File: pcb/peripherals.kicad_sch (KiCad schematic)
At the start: 30 parts, among them U2 PCA9545APW, U3 HDC1080, U4 LTR-303ALS-01, U5 SGP40-D-R4

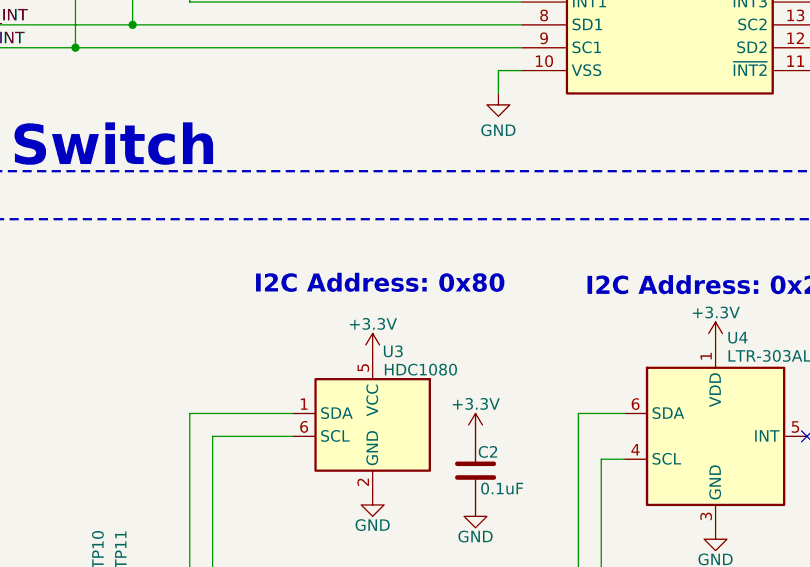
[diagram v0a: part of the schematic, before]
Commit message: Fixed LTR address from 0x80 to 0x40
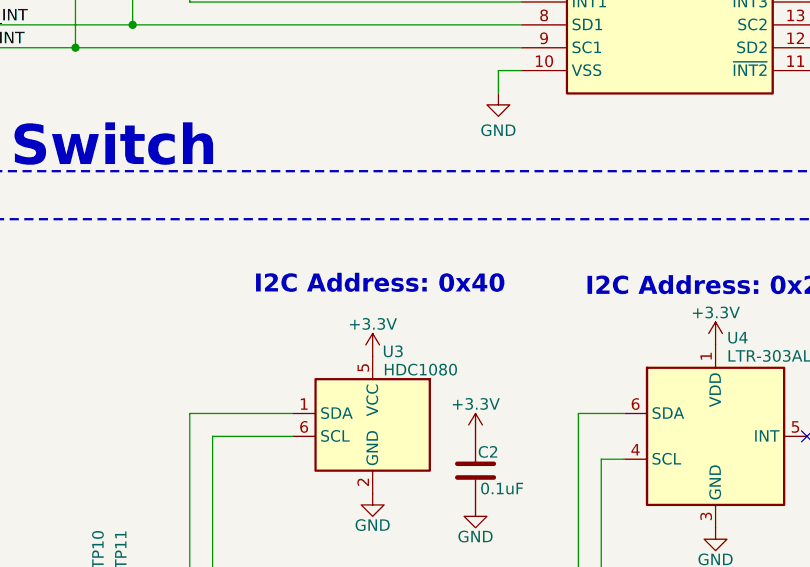
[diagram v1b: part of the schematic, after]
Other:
- note added: "I2C Address: 0x40"
- note removed: "I2C Address: 0x80"
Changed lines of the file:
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@@
 		)
 	)
-	(text "I2C Address: 0x80"
+	(text "I2C Address: 0x40"
 		(exclude_from_sim no)
 		(at 55.372 83.566 0)

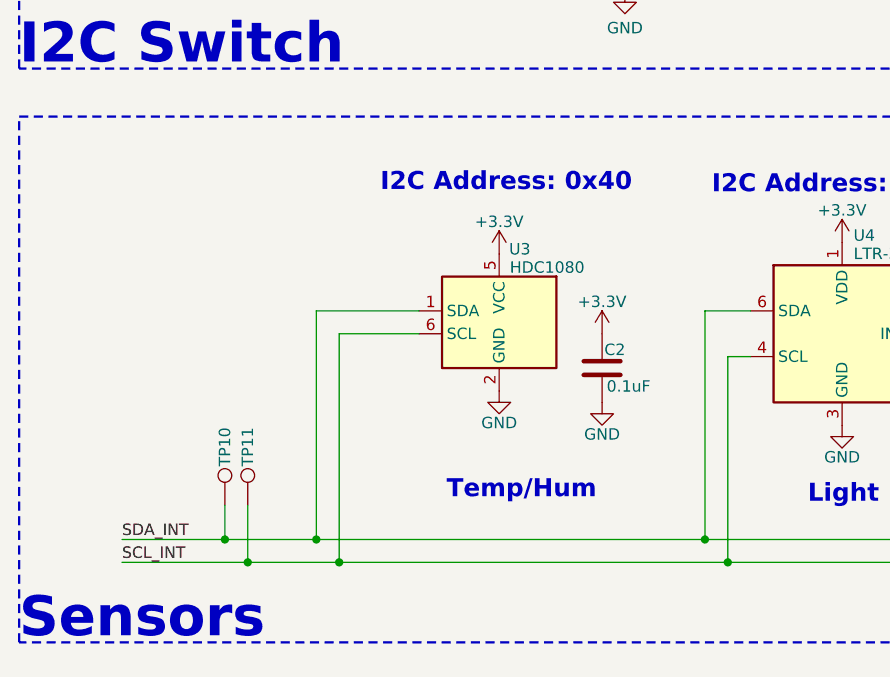
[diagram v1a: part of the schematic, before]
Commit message: Swapped temp sensor for more popular model
Changed HDC1080 for AHT20
Updated reference layer
Updated renders
Updated requirements
Fixed models
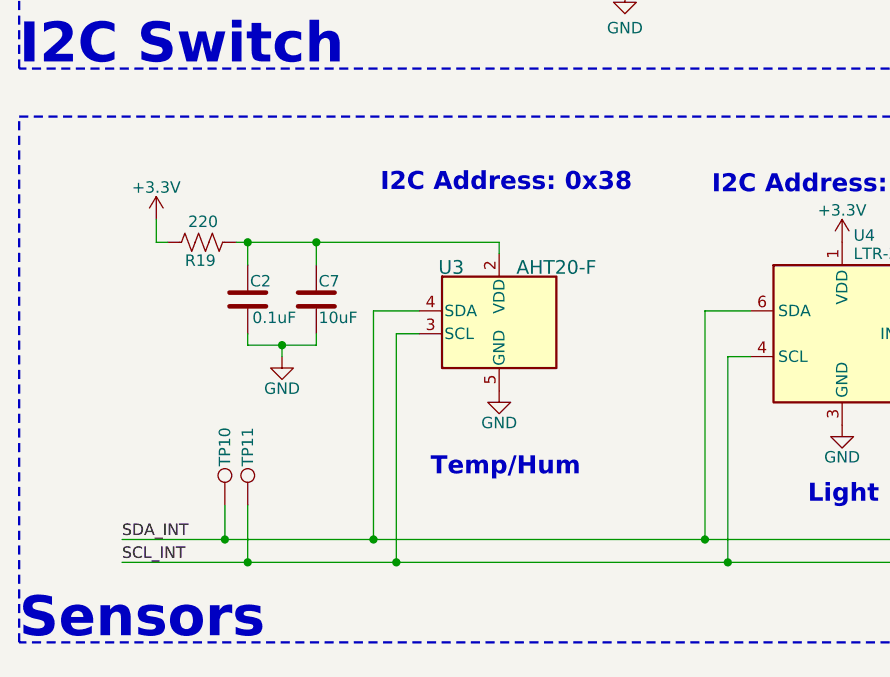
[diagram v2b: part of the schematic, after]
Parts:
- removed U3: HDC1080, CRG Makes:PWSON-N6, symbol CRG Makes:HDC1080
- added C7: 10uF, CRGM Passive:C_0603_1608Metric, symbol Device:C
- added R19: 220, CRGM Passive:R_0603_1608Metric, symbol Device:R_US
- added U3: AHT20-F, CRG Makes:AHT20, symbol CRG Makes:AHT20-F
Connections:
- net +3.3V: now also R19.1; no longer C2.1
- net GND: now also C7.2, U3.5 (GND)
- net SCL_INT: now also U3.3 (SCL)
- net SDA_INT: now also U3.4 (SDA)
- new net: C2.1, C7.1, R19.2, U3.2 (VDD)
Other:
- note added: "I2C Address: 0x38"
- note removed: "I2C Address: 0x40"
- moved on the sheet: C2

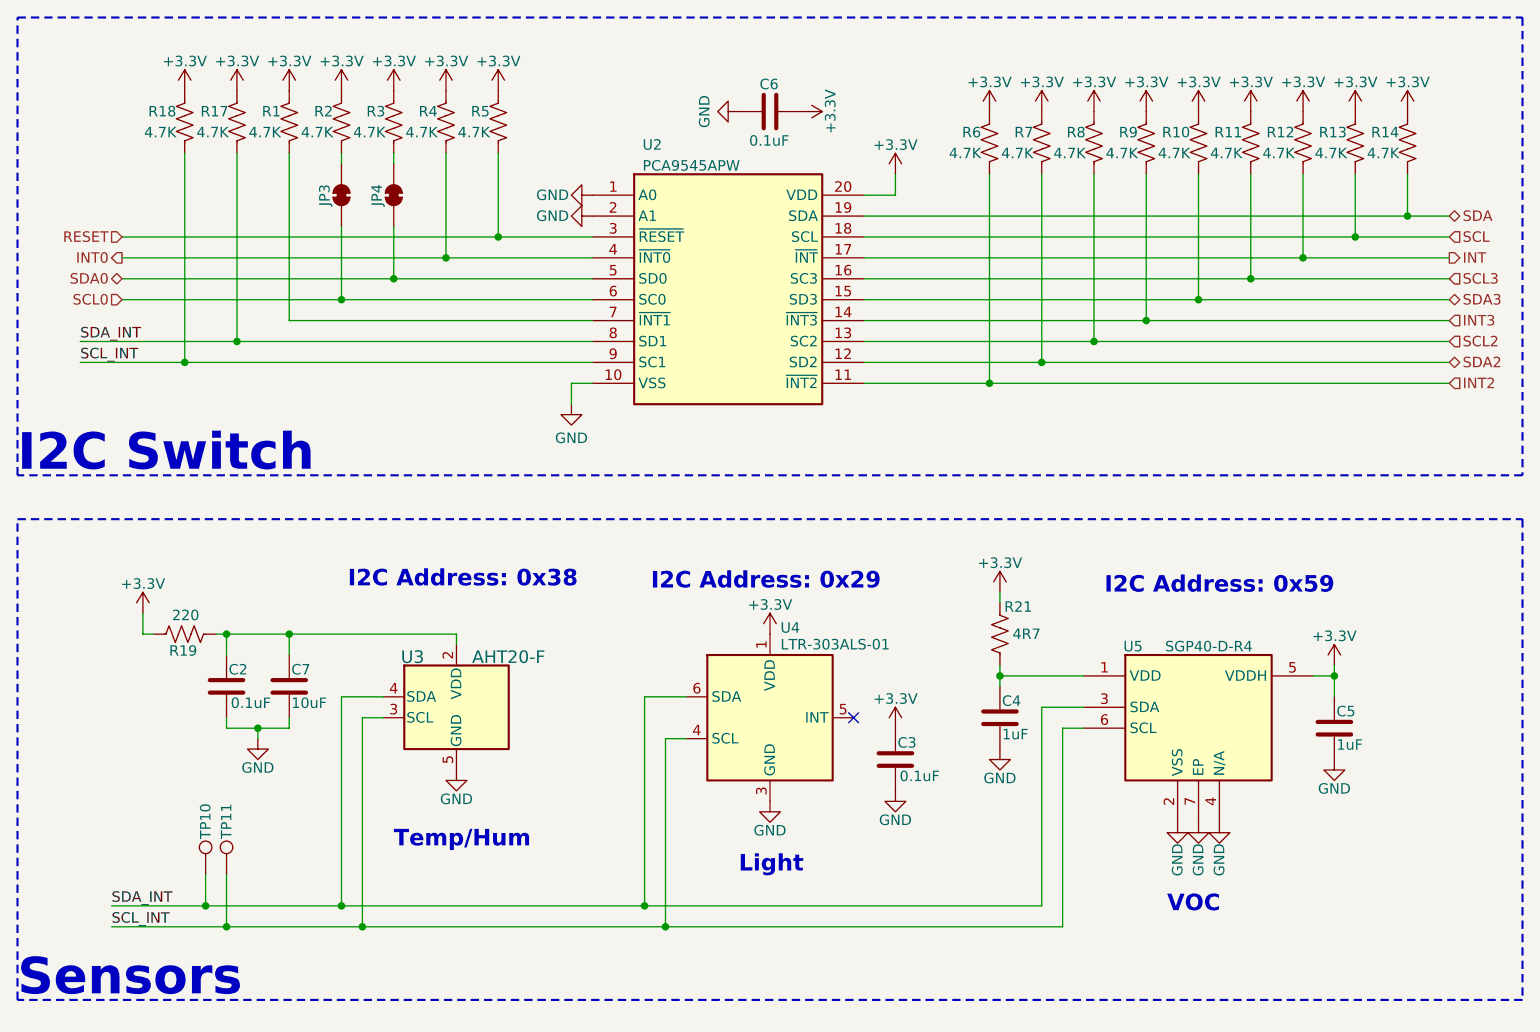
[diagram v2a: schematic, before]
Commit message: Switched back to global lables
Updated all gnd and test point symbols
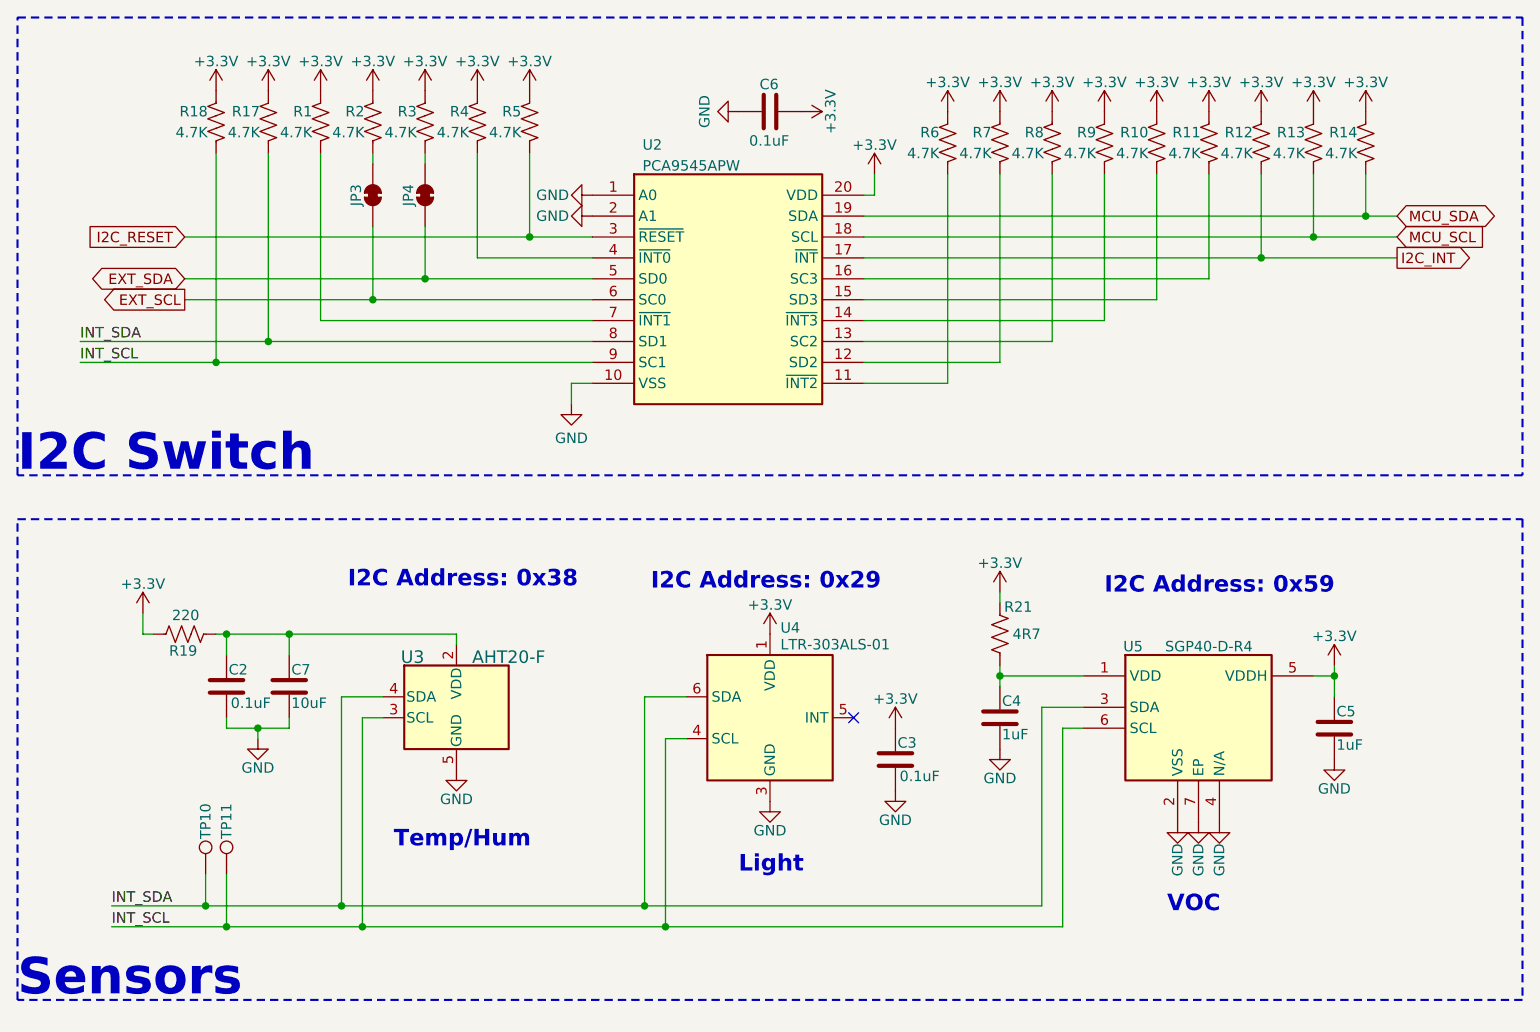
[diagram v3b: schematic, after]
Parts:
- TP10, TP11: symbol Connector:TestPoint -> CRGM Connector:TestPoint
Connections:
- net INT renamed I2C_INT
- net INT0: no longer names the net of R4.1, U2.4 (~{INT0})
- net INT2: no longer names the net of R6.1, U2.11 (~{INT2})
- net INT3: no longer names the net of R9.1, U2.14 (~{INT3})
- net RESET renamed I2C_RESET
- net SCL renamed MCU_SCL
- net SCL0 renamed EXT_SCL
- net SCL2: no longer names the net of R8.1, U2.13 (SC2)
- net SCL3: no longer names the net of R11.1, U2.16 (SC3)
- net SCL_INT renamed INT_SCL
- net SDA renamed MCU_SDA
- net SDA0 renamed EXT_SDA
- net SDA2: no longer names the net of R7.1, U2.12 (SD2)
- net SDA3: no longer names the net of R10.1, U2.15 (SD3)
- net SDA_INT renamed INT_SDA
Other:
- moved on the sheet: JP3, JP4, R1, R10, R11, R12, R13, R14, R17, R18, R2, R3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
